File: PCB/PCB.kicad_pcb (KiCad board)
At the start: 4 copper layers, 25.8 x 62.7 mm, 31 parts, among them U1 ESP32-S3-MINI-1-N8, U2 ESD7104MUTAG, U3 TLV75801PDRV, U4 ENS210

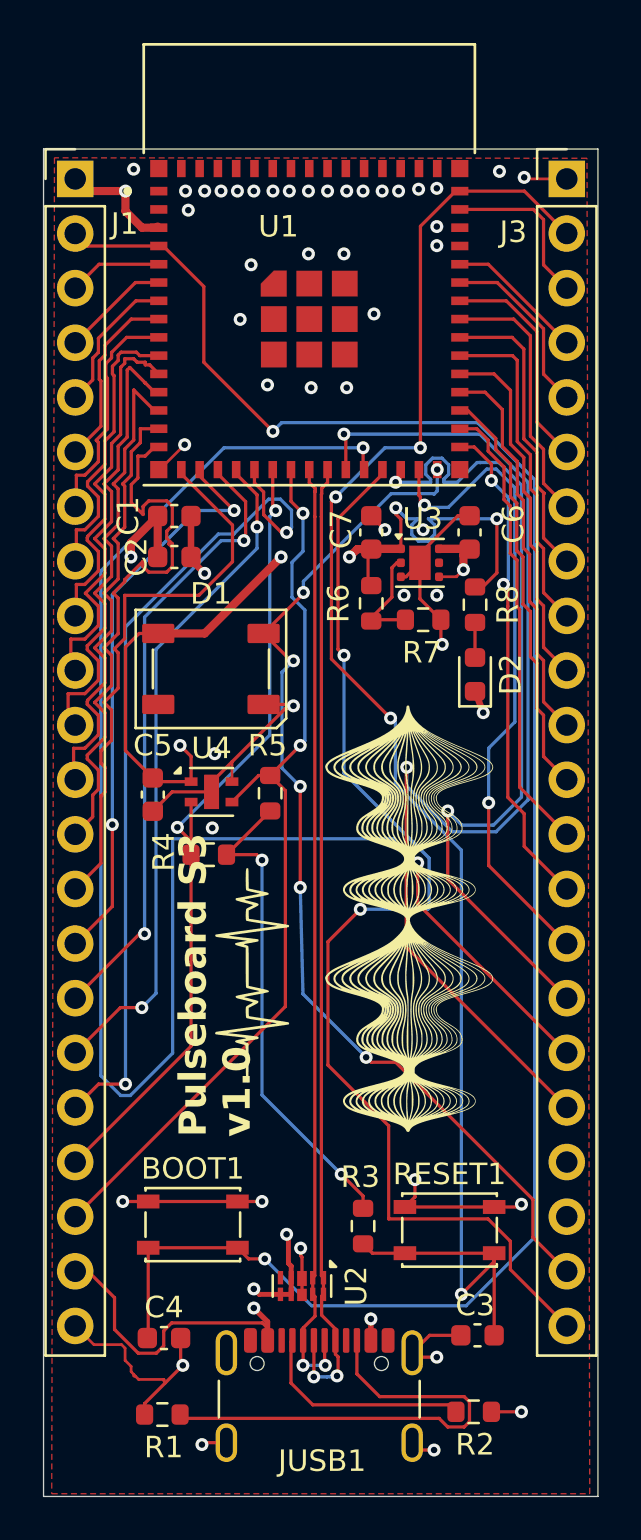
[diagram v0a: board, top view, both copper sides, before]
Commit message: fixed mistake on impdence
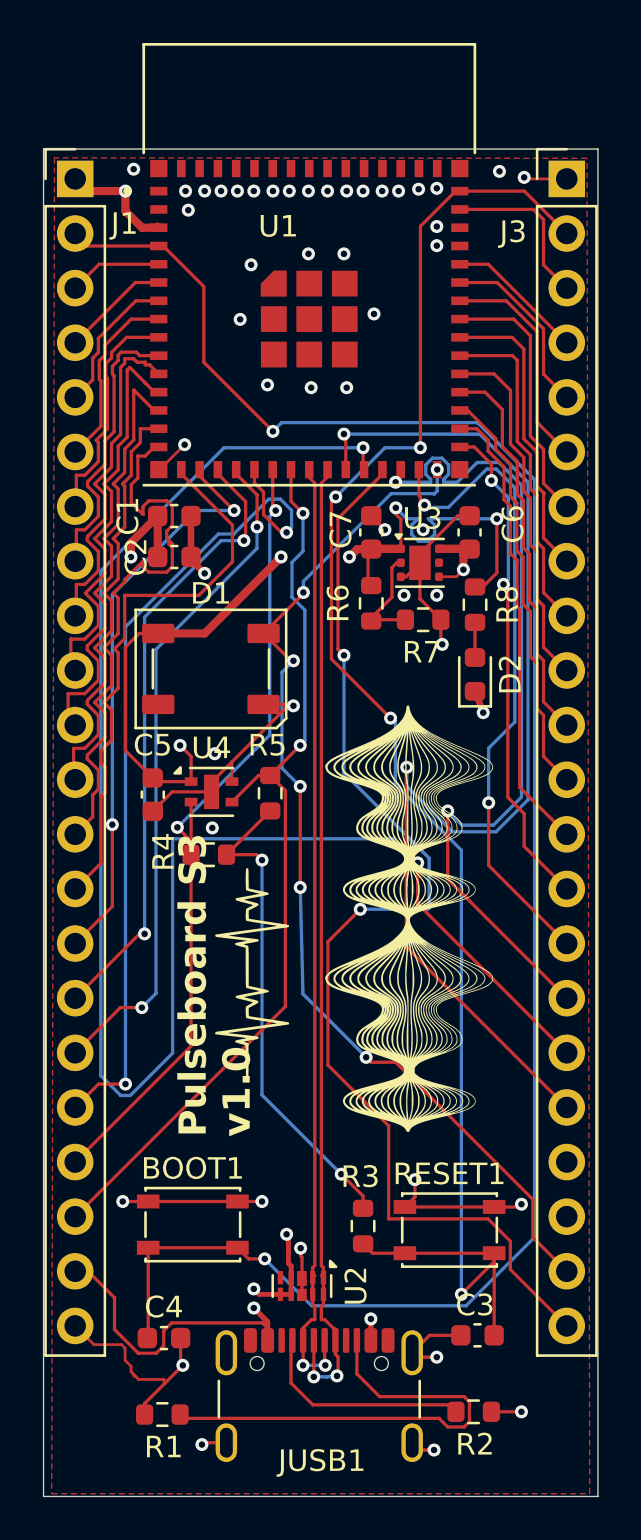
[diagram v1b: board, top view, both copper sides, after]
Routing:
- net /USB_P: track 45.5 -> 46.3 mm
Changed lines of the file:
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@@
 			(plot_on_all_layers_selection 0x00000000_00000000_00000000_00000000)
 			(disableapertmacros no)
-			(usegerberextensions yes)
+			(usegerberextensions no)
 			(usegerberattributes yes)
 			(usegerberadvancedattributes yes)
-			(creategerberjobfile no)
+			(creategerberjobfile yes)
 			(dashed_line_dash_ratio 12.000000)
 			(dashed_line_gap_ratio 3.000000)
@@
 			(drillshape 0)
 			(scaleselection 1)
-			(outputdirectory "")
+			(outputdirectory "../BOM/")
 		)
 	)
@@
 	)
 	(segment
-		(start 125.896 80.229001)
-		(end 126.1686 80.501601)
-		(width 0.1524)
-		(layer "F.Cu")
-		(net 49)
-	)
-	(segment
-		(start 126.1686 80.639859)
-		(end 126.1531 80.655359)
+		(start 126.0555 116.739249)
+		(end 126.1531 116.641649)
 		(width 0.1524)
 		(layer "F.Cu")
@@
 	)
 	(segment
-		(start 126.16 119)
-		(end 126.16 118.0875)
-		(width 0.1524)
-		(layer "F.Cu")
-		(net 49)
-	)
-	(segment
 		(start 126.640999 121.285)
 		(end 126.746 121.179999)
@@
 	)
 	(segment
-		(start 126.153099 81.818201)
-		(end 126.153099 117.110401)
-		(width 0.1524)
+		(start 125.896 79.629)
+		(end 125.896 80.000725)
+		(width 0.141986)
 		(layer "F.Cu")
 		(net 49)
 	)
 	(segment
-		(start 126.1686 80.501601)
-		(end 126.1686 80.639859)
+		(start 126.1531 116.641649)
+		(end 126.1531 80.257825)
 		(width 0.1524)
 		(layer "F.Cu")
@@
 	)
 	(segment
-		(start 126.1531 81.8182)
-		(end 126.153099 81.818201)
+		(start 125.61 119.550001)
+		(end 125.61 120.125)
 		(width 0.1524)
 		(layer "F.Cu")
@@
 	)
 	(segment
-		(start 126.0555 117.983)
-		(end 126.0555 117.208)
+		(start 126.0555 117.208)
+		(end 126.0555 116.739249)
 		(width 0.1524)
 		(layer "F.Cu")
@@
 	)
 	(segment
-		(start 126.746 121.158)
-		(end 126.61 121.022)
+		(start 126.1531 119.16)
+		(end 126.000001 119.16)
 		(width 0.1524)
 		(layer "F.Cu")
@@
 	)
 	(segment
-		(start 126.746 121.179999)
-		(end 126.746 121.158)
+		(start 126.0555 117.983)
+		(end 126.0555 118.451751)
 		(width 0.1524)
 		(layer "F.Cu")
@@
 	)
 	(segment
-		(start 125.61 119.550001)
-		(end 126.16 119)
+		(start 125.896 80.000725)
+		(end 126.1531 80.257825)
+		(width 0.141986)
+		(layer "F.Cu")
+		(net 49)
+	)
+	(segment
+		(start 126.0555 117.983)
+		(end 126.0555 117.208)
 		(width 0.1524)
 		(layer "F.Cu")
@@
 	)
 	(segment
-		(start 125.896 79.629)
-		(end 125.896 80.229001)
+		(start 126.746 121.158)
+		(end 126.61 121.022)
 		(width 0.1524)
 		(layer "F.Cu")
@@
 	)
 	(segment
-		(start 125.604401 121.283765)
-		(end 125.604401 121.2526)
+		(start 126.746 121.179999)
+		(end 126.746 121.158)
 		(width 0.1524)
 		(layer "F.Cu")
@@
 	)
 	(segment
-		(start 126.16 118.0875)
-		(end 126.0555 117.983)
+		(start 126.000001 119.16)
+		(end 125.61 119.550001)
 		(width 0.1524)
 		(layer "F.Cu")
@@
 	)
 	(segment
-		(start 126.1531 80.655359)
-		(end 126.1531 81.8182)
+		(start 126.1531 118.549351)
+		(end 126.1531 119.16)
 		(width 0.1524)
 		(layer "F.Cu")
@@
 	)
 	(segment
-		(start 125.61 120.125)
-		(end 125.61 119.550001)
+		(start 125.604401 121.283765)
+		(end 125.604401 121.2526)
+		(width 0.1524)
+		(layer "F.Cu")
+		(net 49)
+	)
+	(segment
+		(start 126.0555 118.451751)
+		(end 126.1531 118.549351)
 		(width 0.1524)
 		(layer "F.Cu")
@@
 	)
 	(segment
-		(start 126.5555 117.983)
-		(end 126.5555 117.208)
+		(start 126.4579 119.16)
+		(end 126.616926 119.16)
 		(width 0.1524)
 		(layer "F.Cu")
@@
 	)
 	(segment
-		(start 126.4579 81.8182)
-		(end 126.457901 81.818201)
+		(start 126.4579 118.549351)
+		(end 126.4579 119.16)
 		(width 0.1524)
 		(layer "F.Cu")
@@
 	)
 	(segment
-		(start 126.4734 80.7565)
-		(end 126.4579 80.772)
+		(start 126.5555 117.983)
+		(end 126.5555 117.208)
 		(width 0.1524)
 		(layer "F.Cu")
@@
 	)
 	(segment
-		(start 126.47 118.95)
-		(end 126.47 118.0685)
+		(start 126.4579 116.641649)
+		(end 126.4579 80.257825)
 		(width 0.1524)
 		(layer "F.Cu")
@@
 	)
 	(segment
-		(start 126.4734 80.501601)
-		(end 126.4734 80.7565)
+		(start 126.746 79.629)
+		(end 126.746 79.969725)
+		(width 0.141986)
+		(layer "F.Cu")
+		(net 50)
+	)
+	(segment
+		(start 127.11 119.653074)
+		(end 127.11 120.125)
 		(width 0.1524)
 		(layer "F.Cu")
@@
 	)
 	(segment
-		(start 126.47 118.0685)
-		(end 126.5555 117.983)
+		(start 126.616926 119.16)
+		(end 127.11 119.653074)
 		(width 0.1524)
 		(layer "F.Cu")
@@
 	)
 	(segment
-		(start 127.11 119.59)
-		(end 126.47 118.95)
+		(start 126.5555 118.451751)
+		(end 126.4579 118.549351)
 		(width 0.1524)
 		(layer "F.Cu")
@@
 	)
 	(segment
-		(start 126.4579 80.772)
-		(end 126.4579 81.8182)
+		(start 126.5555 117.983)
+		(end 126.5555 118.451751)
 		(width 0.1524)
 		(layer "F.Cu")
@@
 	)
 	(segment
-		(start 126.746 80.229001)
-		(end 126.4734 80.501601)
+		(start 126.457901 117.110401)
+		(end 126.5555 117.208)
 		(width 0.1524)
 		(layer "F.Cu")
@@
 	)
 	(segment
-		(start 126.457901 117.110401)
-		(end 126.5555 117.208)
+		(start 126.5555 116.739249)
+		(end 126.4579 116.641649)
 		(width 0.1524)
 		(layer "F.Cu")
@@
 	)
 	(segment
-		(start 126.746 79.629)
-		(end 126.746 80.229001)
+		(start 126.5555 117.208)
+		(end 126.5555 116.739249)
 		(width 0.1524)
 		(layer "F.Cu")
@@
 	)
 	(segment
-		(start 127.11 120.76)
-		(end 127.11 120.125)
-		(width 0.1524)
+		(start 126.746 79.969725)
+		(end 126.4579 80.257825)
+		(width 0.141986)
 		(layer "F.Cu")
 		(net 50)
 	)
 	(segment
-		(start 126.457901 81.818201)
-		(end 126.457901 117.110401)
+		(start 127.11 120.76)
+		(end 127.11 120.125)
 		(width 0.1524)
 		(layer "F.Cu")
